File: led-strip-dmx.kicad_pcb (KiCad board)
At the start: 2 copper layers, 50 x 100 mm, 38 parts, among them IC1 ATMEGA168-P, IC2 MAX485, IC3 74HC165, P1 POWER_IN, P2 POWER_OUT, P3 ISP, P4 LED_OUT, P5 SIGNAL_IN, P6 SIGNAL_OUT, Q1 IRF640N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

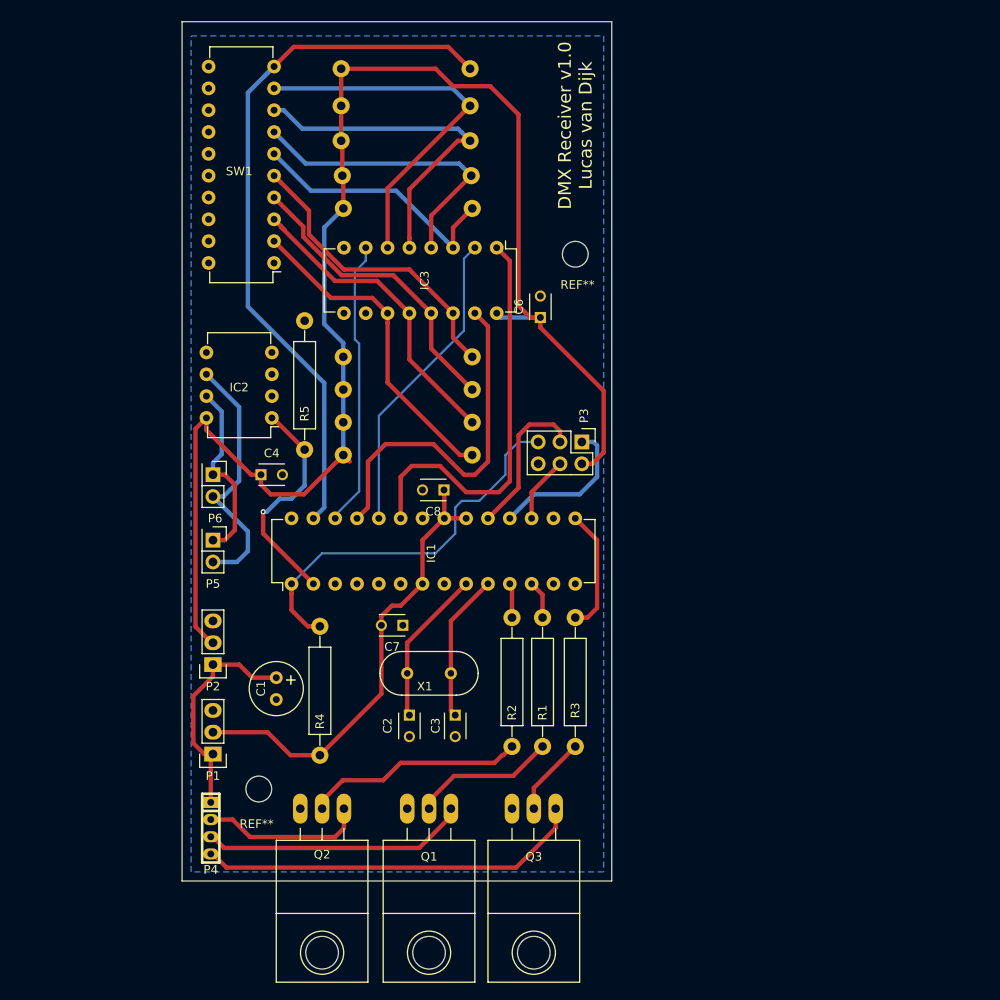
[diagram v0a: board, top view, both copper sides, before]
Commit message: Fix a few major issues on the PCB
- Used wrong pin order for LED transistors
- Right half of the PCB did not get any power
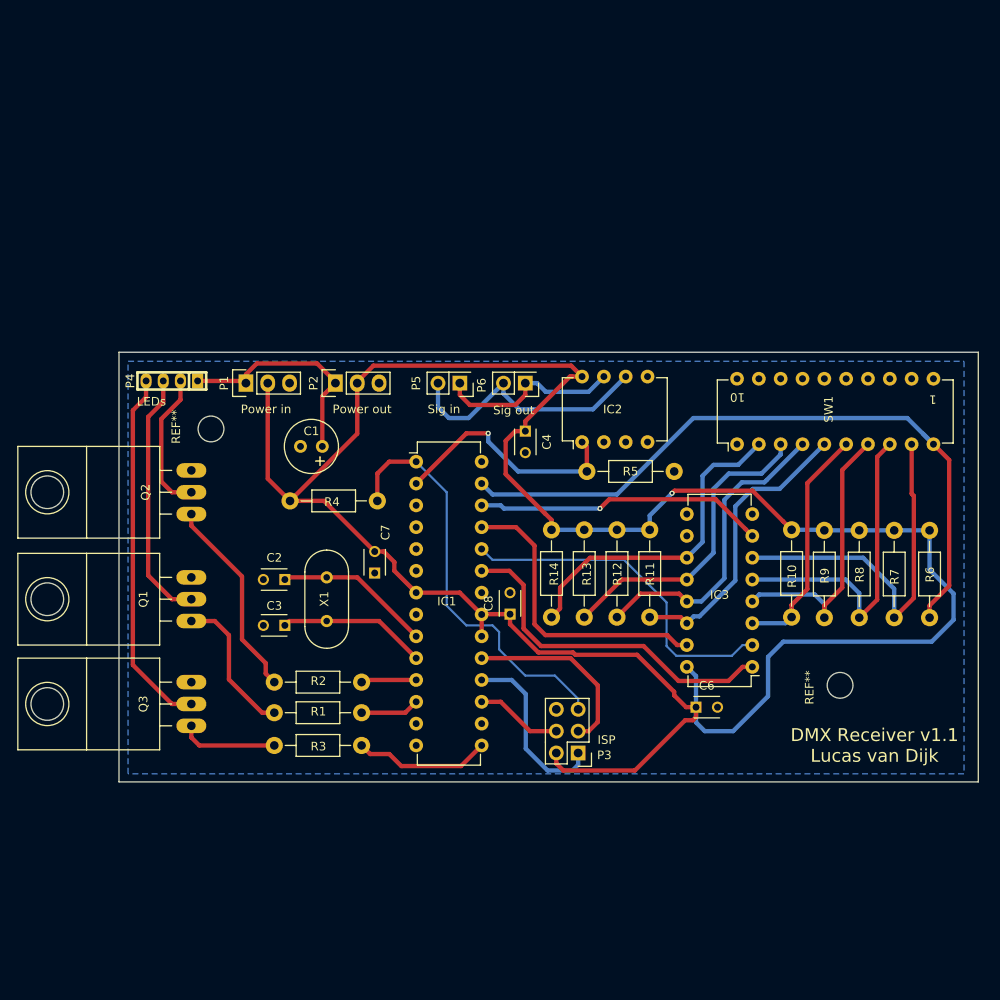
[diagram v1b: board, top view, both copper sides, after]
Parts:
- R1, R2, R3, R4, R5: footprint Resistors_ThroughHole:Resistor_Horizontal_RM15mm -> Resistors_ThroughHole:Resistor_Horizontal_RM10mm
- R10, R11, R12, R13, R14, R6, R7, R8, R9: footprint Resistors_ThroughHole:Resistor_Horizontal_RM15mm -> Resistors_ThroughHole:Resistor_Horizontal_RM10mm; moved to F.Cu
- moved G*** 85.4 mm to (189.6, 127.7), turned to 180 degrees
- moved R6 84.7 mm to (191.2, 110.8), turned to 90 degrees
- moved R7 78.7 mm to (187.1, 110.8), turned to 90 degrees
- moved R8 73.0 mm to (183.0, 110.8), turned to 90 degrees
- moved R9 67.2 mm to (178.9, 110.8), turned to 90 degrees
- moved R10 61.6 mm to (175.1, 110.7), turned to 90 degrees
- moved REF** 58.9 mm to (180.8, 123.7), turned to 0 degrees
- moved SW1 57.9 mm to (168.8, 95.7), turned to 90 degrees
- moved IC3 57.1 mm to (170.5, 121.6), turned to 180 degrees
- moved P4 52.2 mm to (103.0, 88.3), turned to 180 degrees
- moved C6 48.8 mm to (164.0, 126.3), turned to 0 degrees
- moved P1 43.3 mm to (111.6, 88.6), turned to 90 degrees
- moved REF** 42.3 mm to (107.6, 93.9), turned to 0 degrees
- moved Q3 41.7 mm to (105.3, 125.9), turned to 90 degrees
- moved Q2 39.8 mm to (105.3, 101.3), turned to 90 degrees
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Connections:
- Q1 pad 1: /R -> Net-(Q1-Pad1)
- Q1 pad 2: Net-(Q1-Pad2) -> /R
- Q2 pad 1: /G -> Net-(Q2-Pad1)
- Q2 pad 2: Net-(Q2-Pad2) -> /G
- Q3 pad 1: /B -> Net-(Q3-Pad1)
- Q3 pad 2: Net-(Q3-Pad2) -> /B
- R1 pad 2: Net-(Q1-Pad2) -> Net-(Q1-Pad1)
- R10 pad 1: +5V -> /SW4
- R10 pad 2: /SW4 -> +5V
- R11 pad 1: +5V -> /SW3
- R11 pad 2: /SW3 -> +5V
- R12 pad 1: +5V -> /SW2
- R12 pad 2: /SW2 -> +5V
- R13 pad 1: +5V -> /SW1
- R13 pad 2: /SW1 -> +5V
- R14 pad 1: +5V -> /SW0
- R14 pad 2: /SW0 -> +5V
- R2 pad 2: Net-(Q2-Pad2) -> Net-(Q2-Pad1)
- R3 pad 2: Net-(Q3-Pad2) -> Net-(Q3-Pad1)
- R6 pad 1: +5V -> /SW8
- R6 pad 2: /SW8 -> +5V
- R7 pad 1: +5V -> /SW7
- R7 pad 2: /SW7 -> +5V
- R8 pad 1: +5V -> /SW6
- R8 pad 2: /SW6 -> +5V
- R9 pad 1: +5V -> /SW5
- R9 pad 2: /SW5 -> +5V
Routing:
- net +5V: track 227.5 -> 273.3 mm, vias 0 -> 1
- net Net-(Q2-Pad2): track 25.6 -> 0.00 mm
- net Net-(Q2-Pad1): track 0.00 -> 23.6 mm
- net Net-(Q1-Pad1): track 0.00 -> 17.1 mm
- net Net-(Q1-Pad2): track 16.7 -> 0.00 mm
- net Net-(Q3-Pad1): track 0.00 -> 11.4 mm
- net Net-(Q3-Pad2): track 9.95 -> 0.00 mm
- net /PL: track 48.0 -> 40.8 mm
- net /CE: track 42.3 -> 35.3 mm
- net /CP: track 36.1 -> 40.1 mm
- net /SCK: track 18.1 -> 21.8 mm
- net /SW4: track 30.9 -> 27.6 mm
- net /B: track 45.9 -> 42.6 mm
- net /MISO: track 17.8 -> 21.0 mm
- net /SW8: track 85.6 -> 82.7 mm
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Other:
- board size 50 x 100 mm -> 100 x 50 mm
- board text added: "1"
- board text added: "10"
- board text added: "DMX Receiver v1.1 Lucas van Dijk"
- board text added: "ISP"
- board text added: "LEDs"
- board text added: "Power in"
- board text added: "Power out"
- board text added: "Sig in"
- board text added: "Sig out"
- board text removed: "DMX Receiver v1.0 Lucas van Dijk"
